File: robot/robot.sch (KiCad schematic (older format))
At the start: 0 parts

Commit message: Motor driver
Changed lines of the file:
@@
 	4450 2650 4550 2650
 $Sheet
-S 7200 1850 900  800
+S 6900 2550 750  1300
 U 5D63FA00
 F0 "Motor And Driver" 50
 F1 "Motor And Driver.sch" 50
+F2 "M1_AIN1" I L 6900 2800 50
+F3 "M1_AIN2" I L 6900 2900 50
+F4 "M1_BIN1" I L 6900 3000 50
+F5 "M1_BIN2" I L 6900 3100 50
+F6 "M1_SLEEP" I L 6900 2650 50
+F7 "M2_AIN1" I L 6900 3450 50
+F8 "M2_AIN2" I L 6900 3550 50
+F9 "M2_BIN1" I L 6900 3650 50
+F10 "M2_BIN2" I L 6900 3750 50
+F11 "M2_SLEEP" I L 6900 3300 50
 $EndSheet
 $EndSCHEMATC

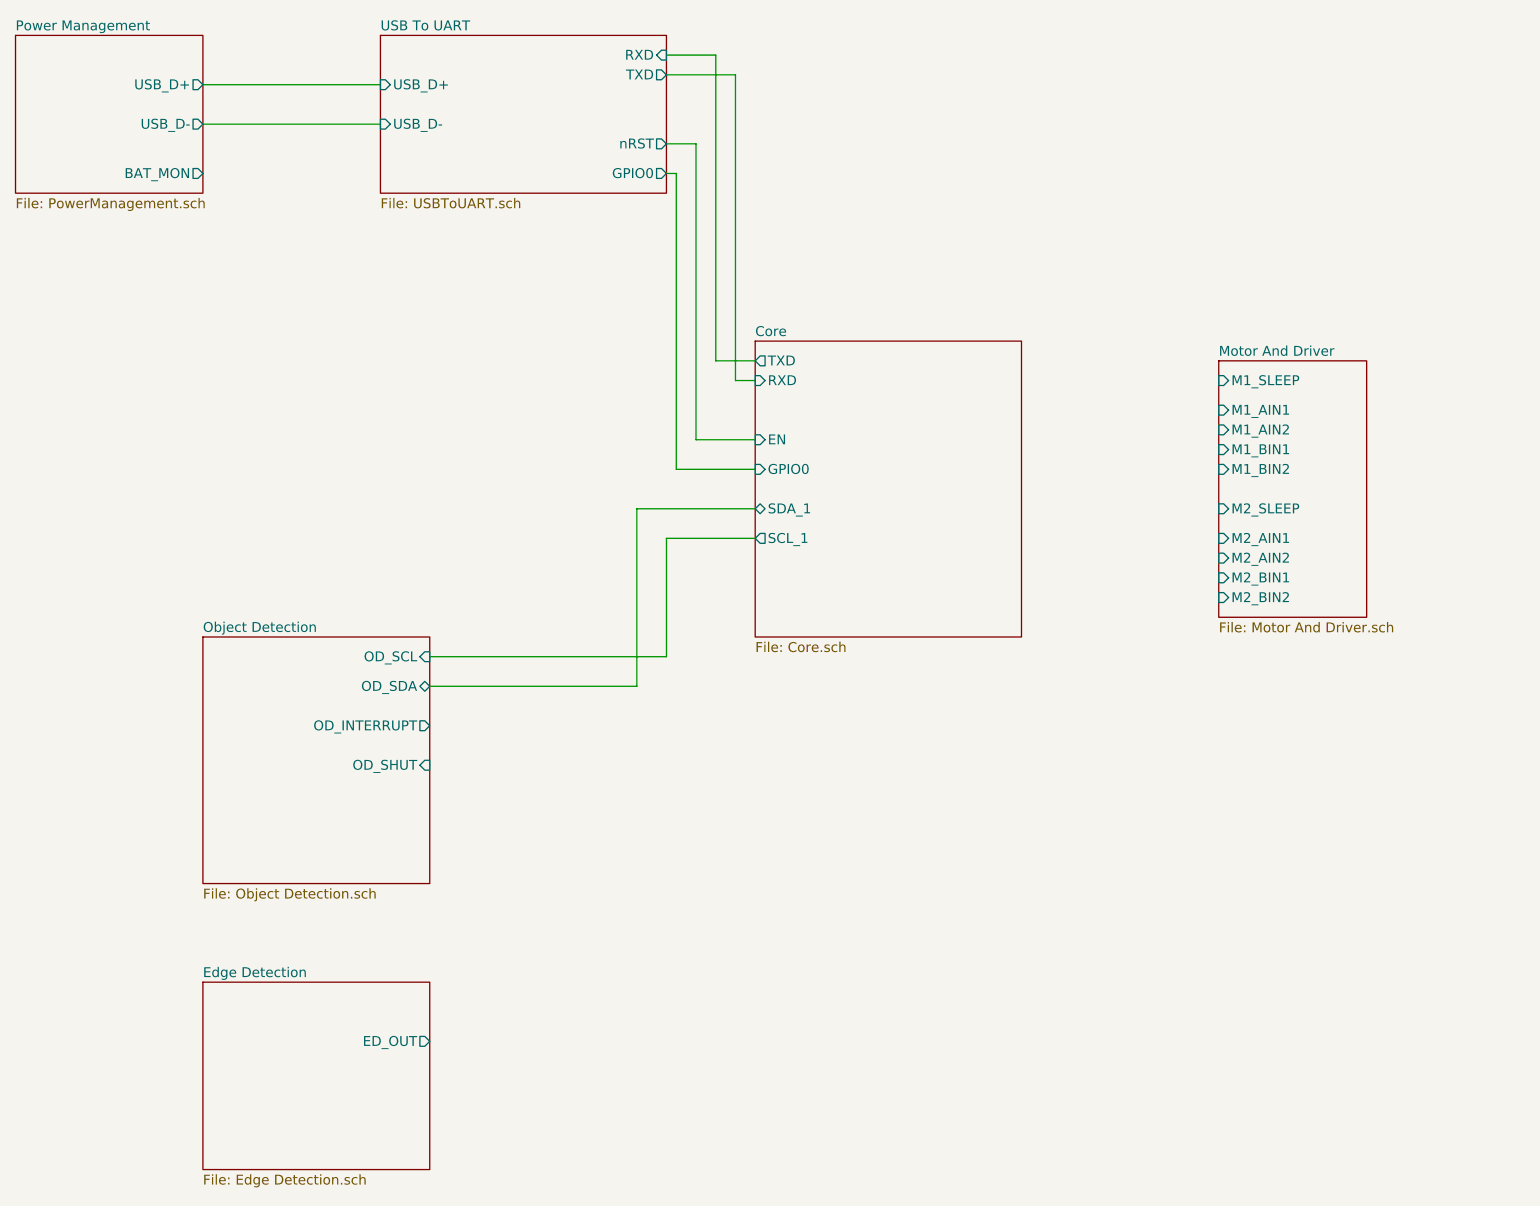
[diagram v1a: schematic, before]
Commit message: UI parts, (re)wiring remaining signals
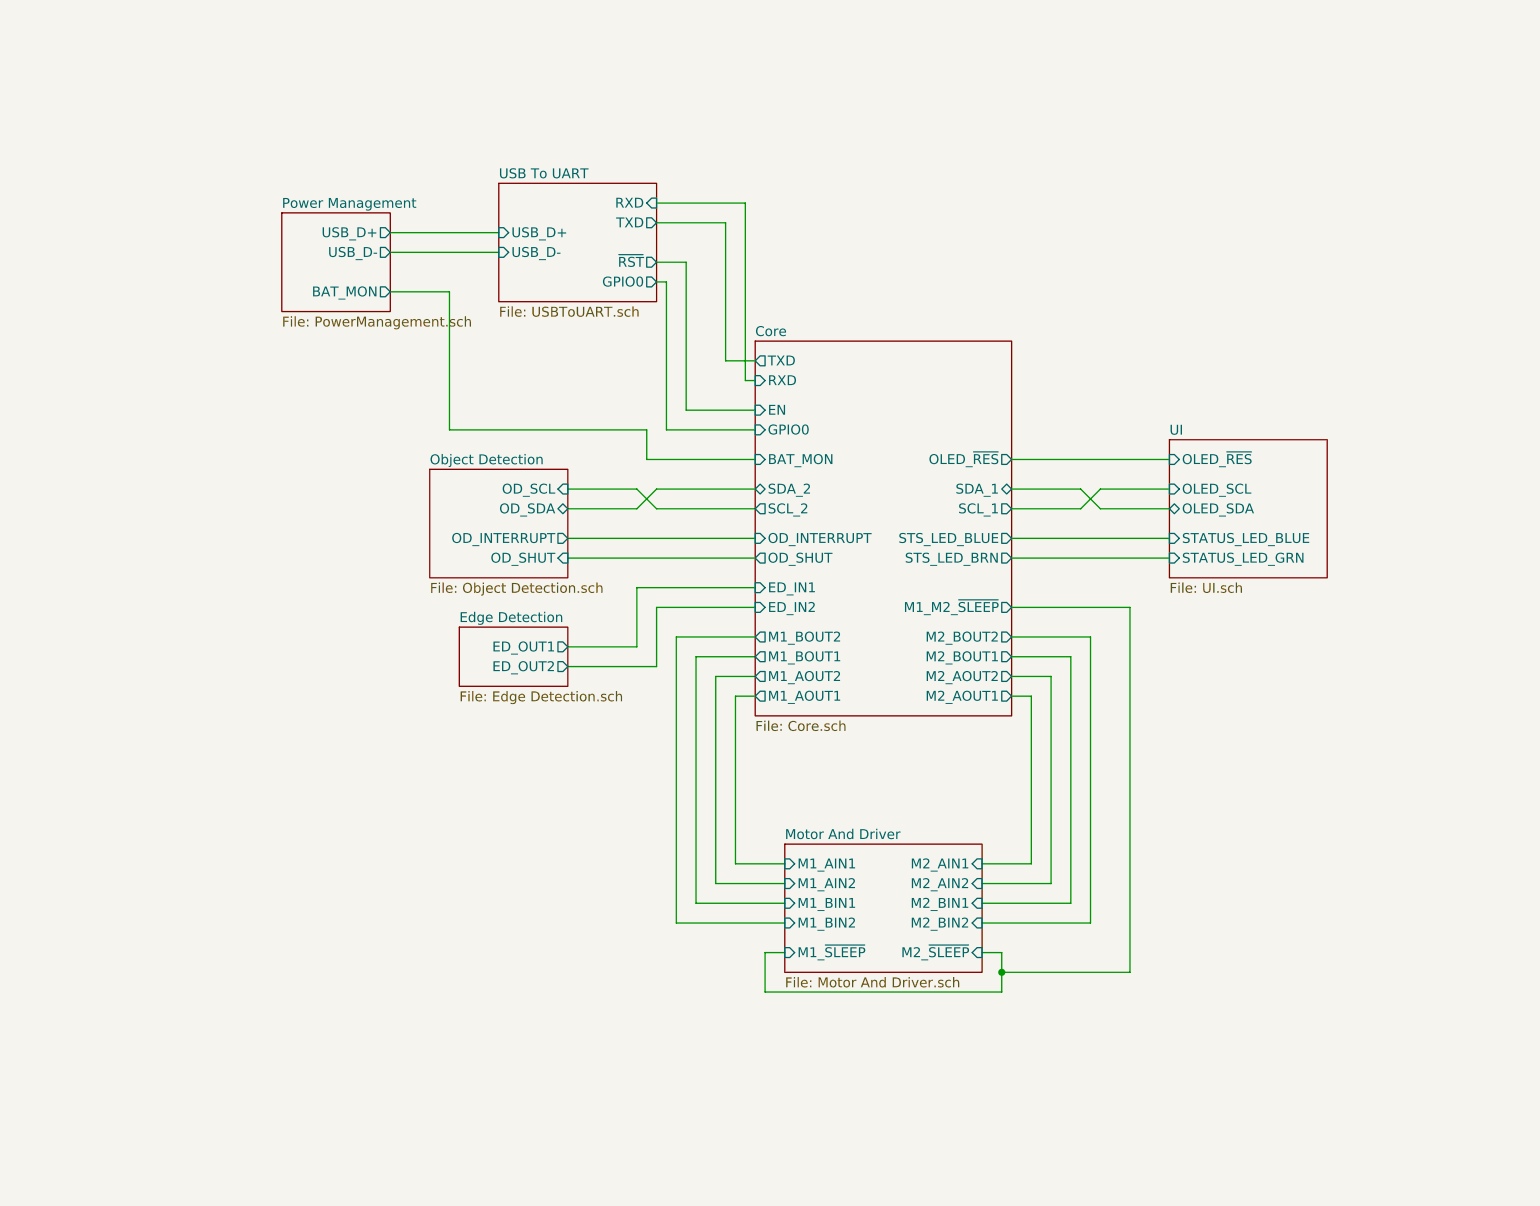
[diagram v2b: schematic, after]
